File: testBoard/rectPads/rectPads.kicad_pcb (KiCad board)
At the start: 2 copper layers, 1 part

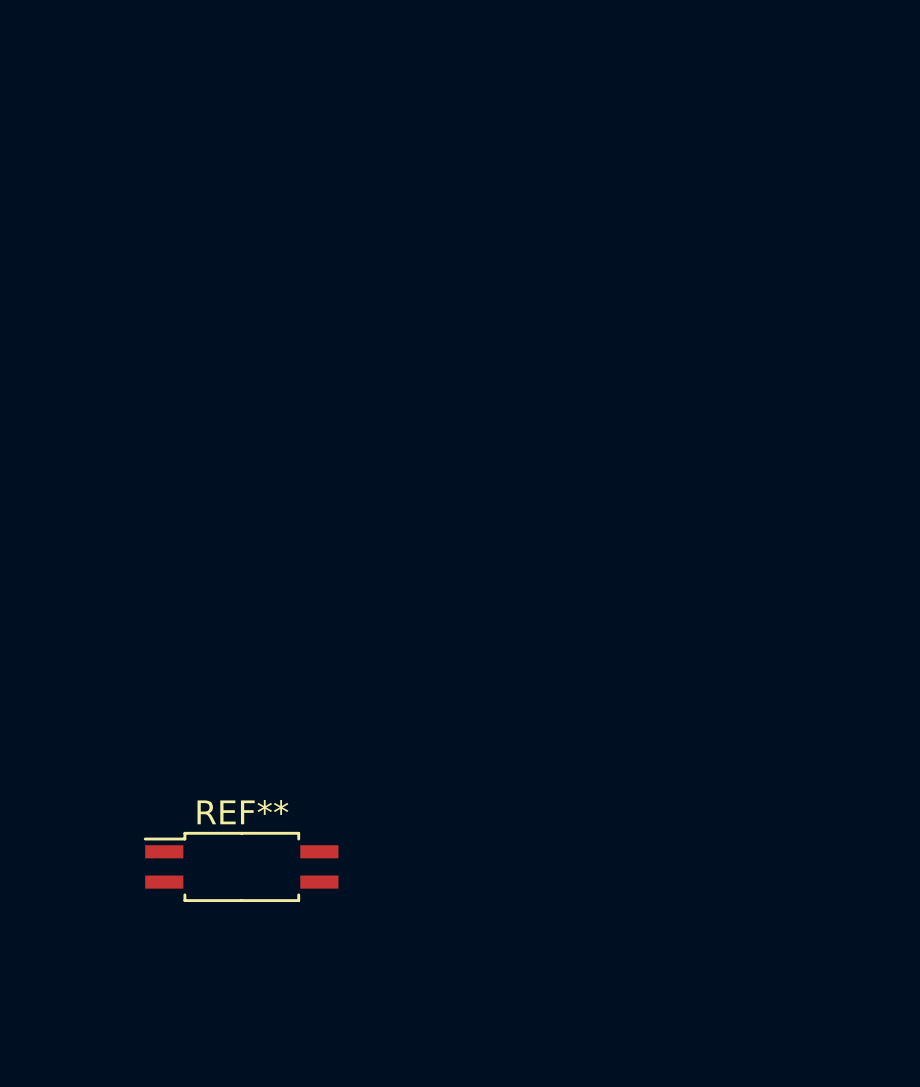
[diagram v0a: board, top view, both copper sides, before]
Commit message: Fix pads drawing errors.
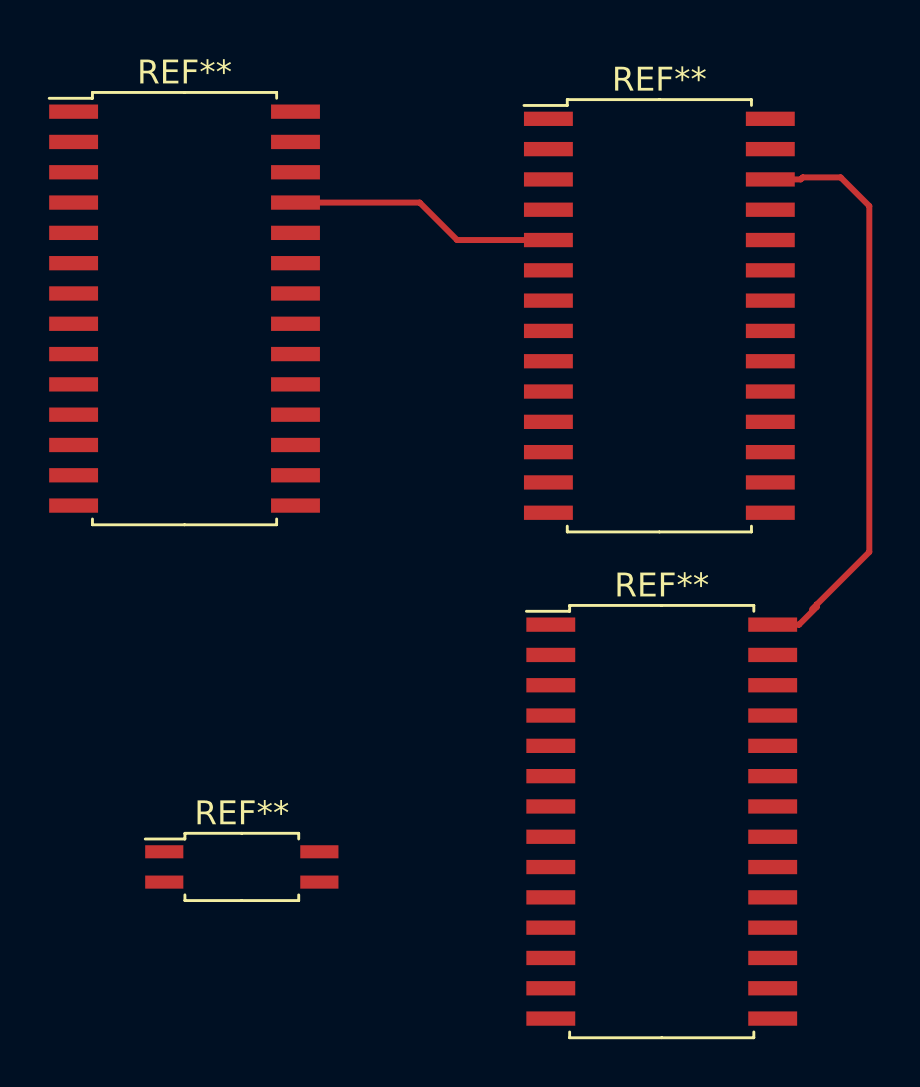
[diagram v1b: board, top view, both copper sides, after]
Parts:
- added REF**: SOIC-28W_7.5x17.9mm_P1.27mm, Package_SO:SOIC-28W_7.5x17.9mm_P1.27mm, F.Cu at (122.8, 58.8)
- added REF**: SOIC-28W_7.5x17.9mm_P1.27mm, Package_SO:SOIC-28W_7.5x17.9mm_P1.27mm, F.Cu at (142.7, 59.1)
- added REF**: SOIC-28W_7.5x17.9mm_P1.27mm, Package_SO:SOIC-28W_7.5x17.9mm_P1.27mm, F.Cu at (142.8, 80.3)
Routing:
- net (no net): track 0.00 -> 36.1 mm
